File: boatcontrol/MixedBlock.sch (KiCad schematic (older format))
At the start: 2 parts, among them U2501 ULN2803A

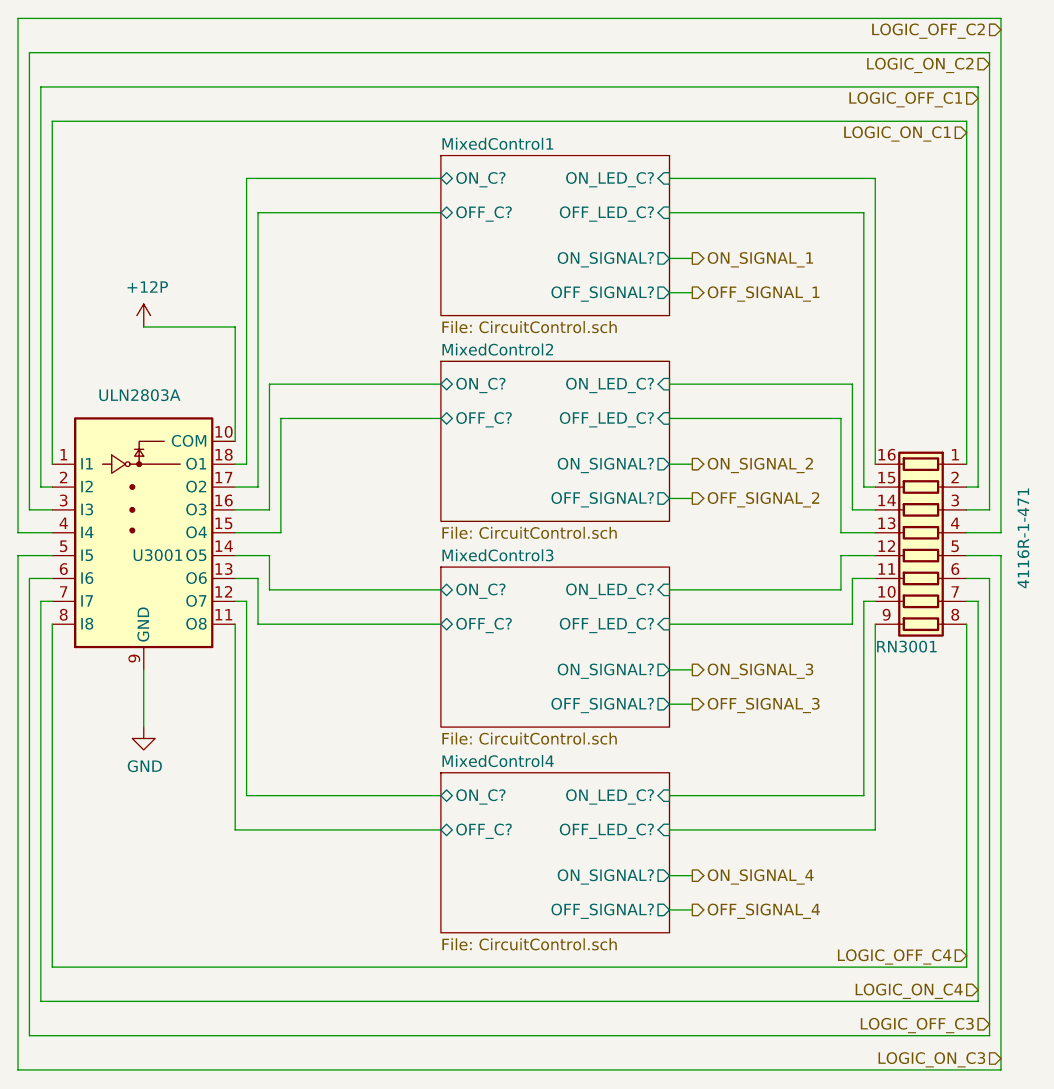
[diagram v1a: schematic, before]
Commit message: Fix extra signals
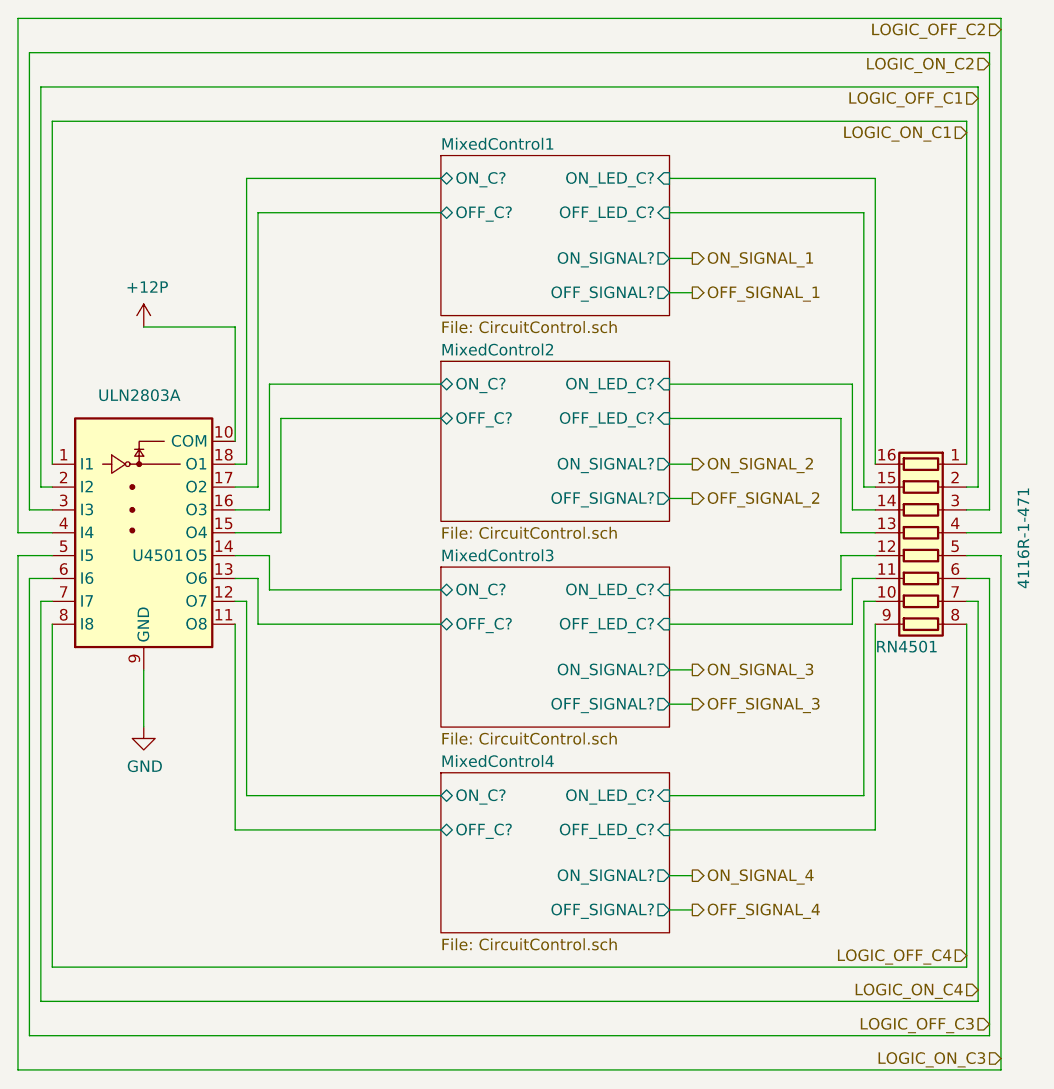
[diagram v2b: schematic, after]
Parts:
- renumbered RN2501 to RN4001, U2501 to U4001
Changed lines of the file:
@@
 AR Path="/E0EE2714/E1383403/E142CD30/D2F31428" Ref="U?"  Part="1"
 AR Path="/E0EE2714/E1383403/E15855D9/D2F31428" Ref="U?"  Part="1"
-AR Path="/E171B33C/E142CD30/D2F31428" Ref="U2501"  Part="1"
-AR Path="/E171B33C/E15855D9/D2F31428" Ref="U3001"  Part="1"
-F 0 "U3001" H 3950 3100 50  0000 L CNN
+AR Path="/E171B33C/E142CD30/D2F31428" Ref="U4001"  Part="1"
+AR Path="/E171B33C/E15855D9/D2F31428" Ref="U4501"  Part="1"
+F 0 "U4501" H 3950 3100 50  0000 L CNN
 F 1 "ULN2803A" H 3800 3800 50  0000 L CNN
 F 2 "Package_DIP:DIP-18_W7.62mm" H 4050 2650 50  0001 L CNN
@@
 AR Path="/E0EE2714/E1383403/E142CD30/5F29B0EF" Ref="#PWR?"  Part="1"
 AR Path="/E0EE2714/E1383403/E15855D9/5F29B0EF" Ref="#PWR?"  Part="1"
-AR Path="/E171B33C/E142CD30/5F29B0EF" Ref="#PWR02502"  Part="1"
-AR Path="/E171B33C/E15855D9/5F29B0EF" Ref="#PWR03002"  Part="1"
-F 0 "#PWR03002" H 4000 4000 50  0001 C CNN
+AR Path="/E171B33C/E142CD30/5F29B0EF" Ref="#PWR04002"  Part="1"
+AR Path="/E171B33C/E15855D9/5F29B0EF" Ref="#PWR04502"  Part="1"
+F 0 "#PWR04502" H 4000 4000 50  0001 C CNN
 F 1 "GND" H 4005 4077 50  0000 C CNN
 F 2 "" H 4000 4250 50  0001 C CNN
@@
 AR Path="/E0EE2714/E1383403/E142CD30/D2B5CDA8" Ref="#PWR?"  Part="1"
 AR Path="/E0EE2714/E1383403/E15855D9/D2B5CDA8" Ref="#PWR?"  Part="1"
-AR Path="/E171B33C/E142CD30/D2B5CDA8" Ref="#PWR02501"  Part="1"
-AR Path="/E171B33C/E15855D9/D2B5CDA8" Ref="#PWR03001"  Part="1"
-F 0 "#PWR03001" H 4000 2350 50  0001 C CNN
+AR Path="/E171B33C/E142CD30/D2B5CDA8" Ref="#PWR04001"  Part="1"
+AR Path="/E171B33C/E15855D9/D2B5CDA8" Ref="#PWR04501"  Part="1"
+F 0 "#PWR04501" H 4000 2350 50  0001 C CNN
 F 1 "+12P" H 4015 2673 50  0000 C CNN
 F 2 "" H 4000 2500 50  0001 C CNN
@@
 AR Path="/E0EE2714/E1383403/E142CD30/D2B5CDA1" Ref="RN?"  Part="1"
 AR Path="/E0EE2714/E1383403/E15855D9/D2B5CDA1" Ref="RN?"  Part="1"
-AR Path="/E171B33C/E142CD30/D2B5CDA1" Ref="RN2501"  Part="1"
-AR Path="/E171B33C/E15855D9/D2B5CDA1" Ref="RN3001"  Part="1"
-F 0 "RN3001" V 7800 3425 50  0000 L CNN
+AR Path="/E171B33C/E142CD30/D2B5CDA1" Ref="RN4001"  Part="1"
+AR Path="/E171B33C/E15855D9/D2B5CDA1" Ref="RN4501"  Part="1"
+F 0 "RN4501" V 7800 3425 50  0000 L CNN
 F 1 "4116R-1-471" H 7100 3050 50  0000 L CNN
 F 2 "BoatControl:DIP254P762X432-16P" V 7875 3500 50  0001 C CNN

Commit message: Cleanup, re-ordering
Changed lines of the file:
@@
 $Descr A4 11693 8268
 encoding utf-8
-Sheet 45 87
+Sheet 40 87
 Title "Boat Control Hat"
 Date "2020-07-09"
@@
 AR Path="/E171B33C/E142CD30/D2F31428" Ref="U4001"  Part="1"
 AR Path="/E171B33C/E15855D9/D2F31428" Ref="U4501"  Part="1"
-F 0 "U4501" H 3950 3100 50  0000 L CNN
+F 0 "U4001" H 3950 3100 50  0000 L CNN
 F 1 "ULN2803A" H 3800 3800 50  0000 L CNN
 F 2 "Package_DIP:DIP-18_W7.62mm" H 4050 2650 50  0001 L CNN
@@
 AR Path="/E171B33C/E142CD30/5F29B0EF" Ref="#PWR04002"  Part="1"
 AR Path="/E171B33C/E15855D9/5F29B0EF" Ref="#PWR04502"  Part="1"
-F 0 "#PWR04502" H 4000 4000 50  0001 C CNN
+F 0 "#PWR04002" H 4000 4000 50  0001 C CNN
 F 1 "GND" H 4005 4077 50  0000 C CNN
 F 2 "" H 4000 4250 50  0001 C CNN
@@
 AR Path="/E171B33C/E142CD30/D2B5CDA8" Ref="#PWR04001"  Part="1"
 AR Path="/E171B33C/E15855D9/D2B5CDA8" Ref="#PWR04501"  Part="1"
-F 0 "#PWR04501" H 4000 2350 50  0001 C CNN
+F 0 "#PWR04001" H 4000 2350 50  0001 C CNN
 F 1 "+12P" H 4015 2673 50  0000 C CNN
 F 2 "" H 4000 2500 50  0001 C CNN
@@
 AR Path="/E171B33C/E142CD30/D2B5CDA1" Ref="RN4001"  Part="1"
 AR Path="/E171B33C/E15855D9/D2B5CDA1" Ref="RN4501"  Part="1"
-F 0 "RN4501" V 7800 3425 50  0000 L CNN
+F 0 "RN4001" V 7800 3425 50  0000 L CNN
 F 1 "4116R-1-471" H 7100 3050 50  0000 L CNN
 F 2 "BoatControl:DIP254P762X432-16P" V 7875 3500 50  0001 C CNN

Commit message: Fix up 10/16A
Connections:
- net MixedControl2/ON_C?: no longer U4001.16 (O3)
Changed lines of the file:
@@
 	4550 3300 4550 2750
-Wire Wire Line
-	4550 2750 5300 2750
 Wire Wire Line
 	4400 3200 4500 3200

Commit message: Cleaner flow
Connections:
- net MixedControl2/DIG_ON: now reaches U4001.16 (O3)
- net MixedControl1/OFF_C? renamed MixedControl1/DIG_OFF
- net MixedControl1/OFF_LED_C? renamed MixedControl1/OFF_LED
- net MixedControl1/ON_C? renamed MixedControl1/DIG_ON
- net MixedControl1/ON_LED_C? renamed MixedControl1/ON_LED
- net MixedControl2/OFF_C? renamed MixedControl2/DIG_OFF
- net MixedControl2/OFF_LED_C? renamed MixedControl2/OFF_LED
- net MixedControl2/ON_LED_C? renamed MixedControl2/ON_LED
- net MixedControl3/OFF_C? renamed MixedControl3/DIG_OFF
- net MixedControl3/OFF_LED_C? renamed MixedControl3/OFF_LED
- net MixedControl3/ON_C? renamed MixedControl3/DIG_ON
- net MixedControl3/ON_LED_C? renamed MixedControl3/ON_LED
- net MixedControl4/OFF_C? renamed MixedControl4/DIG_OFF
- net MixedControl4/OFF_LED_C? renamed MixedControl4/OFF_LED
- net MixedControl4/ON_C? renamed MixedControl4/DIG_ON
- net MixedControl4/ON_LED_C? renamed MixedControl4/ON_LED
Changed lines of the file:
@@
 $Descr A4 11693 8268
 encoding utf-8
-Sheet 40 87
+Sheet 45 87
 Title "Boat Control Hat"
 Date "2020-07-09"
@@
 AR Path="/E171B33C/E142CD30/D2F31428" Ref="U4001"  Part="1"
 AR Path="/E171B33C/E15855D9/D2F31428" Ref="U4501"  Part="1"
-F 0 "U4001" H 3950 3100 50  0000 L CNN
+F 0 "U4501" H 3950 3100 50  0000 L CNN
 F 1 "ULN2803A" H 3800 3800 50  0000 L CNN
 F 2 "Package_DIP:DIP-18_W7.62mm" H 4050 2650 50  0001 L CNN
@@
 AR Path="/E171B33C/E142CD30/5F29B0EF" Ref="#PWR04002"  Part="1"
 AR Path="/E171B33C/E15855D9/5F29B0EF" Ref="#PWR04502"  Part="1"
-F 0 "#PWR04002" H 4000 4000 50  0001 C CNN
+F 0 "#PWR04502" H 4000 4000 50  0001 C CNN
 F 1 "GND" H 4005 4077 50  0000 C CNN
 F 2 "" H 4000 4250 50  0001 C CNN
@@
 AR Path="/E171B33C/E142CD30/D2B5CDA8" Ref="#PWR04001"  Part="1"
 AR Path="/E171B33C/E15855D9/D2B5CDA8" Ref="#PWR04501"  Part="1"
-F 0 "#PWR04001" H 4000 2350 50  0001 C CNN
+F 0 "#PWR04501" H 4000 2350 50  0001 C CNN
 F 1 "+12P" H 4015 2673 50  0000 C CNN
 F 2 "" H 4000 2500 50  0001 C CNN
@@
 AR Path="/E171B33C/E142CD30/D2B5CDA1" Ref="RN4001"  Part="1"
 AR Path="/E171B33C/E15855D9/D2B5CDA1" Ref="RN4501"  Part="1"
-F 0 "RN4001" V 7800 3425 50  0000 L CNN
+F 0 "RN4501" V 6850 3350 50  0000 L CNN
 F 1 "4116R-1-471" H 7100 3050 50  0000 L CNN
 F 2 "BoatControl:DIP254P762X432-16P" V 7875 3500 50  0001 C CNN
@@
 F0 "MixedControl1" 50
 F1 "CircuitControl.sch" 50
-F2 "ON_LED_C?" I R 6300 1850 50
-F3 "OFF_LED_C?" I R 6300 2000 50
-F4 "ON_C?" B L 5300 1850 50
-F5 "OFF_C?" B L 5300 2000 50
-F6 "OFF_SIGNAL?" O R 6300 2350 50
-F7 "ON_SIGNAL?" O R 6300 2200 50
-$EndSheet
-$Sheet
-S 5300 2650 1000 700
-U E150AEB9
-F0 "MixedControl2" 50
-F1 "CircuitControl.sch" 50
-F2 "ON_LED_C?" I R 6300 2750 50
-F3 "OFF_LED_C?" I R 6300 2900 50
-F4 "ON_C?" B L 5300 2750 50
-F5 "OFF_C?" B L 5300 2900 50
-F6 "OFF_SIGNAL?" O R 6300 3250 50
-F7 "ON_SIGNAL?" O R 6300 3100 50
+F2 "ON_LED" I R 6300 1850 50
+F3 "OFF_LED" I R 6300 2000 50
+F4 "DIG_ON" B L 5300 1850 50
+F5 "DIG_OFF" B L 5300 2000 50
+F6 "OFF" O R 6300 2350 50
+F7 "ON" O R 6300 2200 50
 $EndSheet
 $Sheet
@@
 F0 "MixedControl3" 50
 F1 "CircuitControl.sch" 50
-F2 "ON_LED_C?" I R 6300 3650 50
-F3 "OFF_LED_C?" I R 6300 3800 50
-F4 "ON_C?" B L 5300 3650 50
-F5 "OFF_C?" B L 5300 3800 50
-F6 "OFF_SIGNAL?" O R 6300 4150 50
-F7 "ON_SIGNAL?" O R 6300 4000 50
+F2 "ON_LED" I R 6300 3650 50
+F3 "OFF_LED" I R 6300 3800 50
+F4 "DIG_ON" B L 5300 3650 50
+F5 "DIG_OFF" B L 5300 3800 50
+F6 "OFF" O R 6300 4150 50
+F7 "ON" O R 6300 4000 50
 $EndSheet
 $Sheet
@@
 F0 "MixedControl4" 50
 F1 "CircuitControl.sch" 50
-F2 "ON_LED_C?" I R 6300 4550 50
-F3 "OFF_LED_C?" I R 6300 4700 50
-F4 "ON_C?" B L 5300 4550 50
-F5 "OFF_C?" B L 5300 4700 50
-F6 "OFF_SIGNAL?" O R 6300 5050 50
-F7 "ON_SIGNAL?" O R 6300 4900 50
+F2 "ON_LED" I R 6300 4550 50
+F3 "OFF_LED" I R 6300 4700 50
+F4 "DIG_ON" B L 5300 4550 50
+F5 "DIG_OFF" B L 5300 4700 50
+F6 "OFF" O R 6300 5050 50
+F7 "ON" O R 6300 4900 50
 $EndSheet
 Text HLabel 6400 2200 2    50   Output ~ 0
@@
 Wire Wire Line
 	6300 5050 6400 5050
+$Sheet
+S 5300 2650 1000 700
+U E150AEB9
+F0 "MixedControl2" 50
+F1 "CircuitControl.sch" 50
+F2 "ON_LED" I R 6300 2750 50
+F3 "OFF_LED" I R 6300 2900 50
+F4 "DIG_ON" B L 5300 2750 50
+F5 "DIG_OFF" B L 5300 2900 50
+F6 "OFF" O R 6300 3250 50
+F7 "ON" O R 6300 3100 50
+$EndSheet
+Wire Wire Line
+	4550 2750 5300 2750
 $EndSCHEMATC

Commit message: Change inductors
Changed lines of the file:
@@
 $Descr A4 11693 8268
 encoding utf-8
-Sheet 45 87
+Sheet 40 87
 Title "Boat Control Hat"
 Date "2020-07-09"
@@
 AR Path="/E171B33C/E142CD30/D2F31428" Ref="U4001"  Part="1"
 AR Path="/E171B33C/E15855D9/D2F31428" Ref="U4501"  Part="1"
-F 0 "U4501" H 3950 3100 50  0000 L CNN
+F 0 "U4001" H 3950 3100 50  0000 L CNN
 F 1 "ULN2803A" H 3800 3800 50  0000 L CNN
 F 2 "Package_DIP:DIP-18_W7.62mm" H 4050 2650 50  0001 L CNN
@@
 AR Path="/E171B33C/E142CD30/5F29B0EF" Ref="#PWR04002"  Part="1"
 AR Path="/E171B33C/E15855D9/5F29B0EF" Ref="#PWR04502"  Part="1"
-F 0 "#PWR04502" H 4000 4000 50  0001 C CNN
+F 0 "#PWR04002" H 4000 4000 50  0001 C CNN
 F 1 "GND" H 4005 4077 50  0000 C CNN
 F 2 "" H 4000 4250 50  0001 C CNN
@@
 AR Path="/E171B33C/E142CD30/D2B5CDA8" Ref="#PWR04001"  Part="1"
 AR Path="/E171B33C/E15855D9/D2B5CDA8" Ref="#PWR04501"  Part="1"
-F 0 "#PWR04501" H 4000 2350 50  0001 C CNN
+F 0 "#PWR04001" H 4000 2350 50  0001 C CNN
 F 1 "+12P" H 4015 2673 50  0000 C CNN
 F 2 "" H 4000 2500 50  0001 C CNN
@@
 AR Path="/E171B33C/E142CD30/D2B5CDA1" Ref="RN4001"  Part="1"
 AR Path="/E171B33C/E15855D9/D2B5CDA1" Ref="RN4501"  Part="1"
-F 0 "RN4501" V 6850 3350 50  0000 L CNN
+F 0 "RN4001" V 6850 3350 50  0000 L CNN
 F 1 "4116R-1-471" H 7100 3050 50  0000 L CNN
 F 2 "BoatControl:DIP254P762X432-16P" V 7875 3500 50  0001 C CNN

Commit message: Swich drivers for big relays
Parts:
- U4001: value ULN2803A -> TBD62783APG; symbol Transistor_Array:ULN2803A -> Transistor_Array:TBD62783A
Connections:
- net +12P: now also U4001.9 (VCC); no longer U4001.10 (COM)
- net GND: now also U4001.10 (GND); no longer U4001.9 (GND)
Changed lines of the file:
@@
 $Descr A4 11693 8268
 encoding utf-8
-Sheet 40 87
+Sheet 45 87
 Title "Boat Control Hat"
 Date "2020-07-09"
@@
 $EndDescr
 $Comp
-L Transistor_Array:ULN2803A U?
+L Transistor_Array:TBD62783A U?
 U 1 1 D2F31428
-P 4000 3300
+P 4000 3400
 AR Path="/D2F31428" Ref="U?"  Part="1"
 AR Path="/8148B1BC/D2F31428" Ref="U?"  Part="1"
@@
 AR Path="/E171B33C/E142CD30/D2F31428" Ref="U4001"  Part="1"
 AR Path="/E171B33C/E15855D9/D2F31428" Ref="U4501"  Part="1"
-F 0 "U4001" H 3950 3100 50  0000 L CNN
-F 1 "ULN2803A" H 3800 3800 50  0000 L CNN
-F 2 "Package_DIP:DIP-18_W7.62mm" H 4050 2650 50  0001 L CNN
-F 3 "http://www.ti.com/lit/ds/symlink/uln2803a.pdf" H 4100 3100 50  0001 C CNN
-	1    4000 3300
+F 0 "U4501" V 4100 3300 50  0000 L CNN
+F 1 "TBD62783APG" V 3850 3150 50  0000 L CNN
+F 2 "Package_DIP:DIP-18_W7.62mm" H 4050 2750 50  0001 L CNN
+F 3 "https://toshiba.semicon-storage.com/info/docget.jsp?did=30523&prodName=TBD62783AFG" H 4100 3200 50  0001 C CNN
+	1    4000 3400
 	1    0    0    -1
 $EndComp
@@
 AR Path="/E171B33C/E142CD30/5F29B0EF" Ref="#PWR04002"  Part="1"
 AR Path="/E171B33C/E15855D9/5F29B0EF" Ref="#PWR04502"  Part="1"
-F 0 "#PWR04002" H 4000 4000 50  0001 C CNN
+F 0 "#PWR04502" H 4000 4000 50  0001 C CNN
 F 1 "GND" H 4005 4077 50  0000 C CNN
 F 2 "" H 4000 4250 50  0001 C CNN
@@
 L power:+12P #PWR?
 U 1 1 D2B5CDA8
-P 4000 2500
+P 4000 2900
 AR Path="/8148B1BC/D2B5CDA8" Ref="#PWR?"  Part="1"
 AR Path="/81CB63BE/D2B5CDA8" Ref="#PWR?"  Part="1"
@@
 AR Path="/E171B33C/E142CD30/D2B5CDA8" Ref="#PWR04001"  Part="1"
 AR Path="/E171B33C/E15855D9/D2B5CDA8" Ref="#PWR04501"  Part="1"
-F 0 "#PWR04001" H 4000 2350 50  0001 C CNN
-F 1 "+12P" H 4015 2673 50  0000 C CNN
-F 2 "" H 4000 2500 50  0001 C CNN
-F 3 "" H 4000 2500 50  0001 C CNN
-	1    4000 2500
+F 0 "#PWR04501" H 4000 2750 50  0001 C CNN
+F 1 "+12P" H 4015 3073 50  0000 C CNN
+F 2 "" H 4000 2900 50  0001 C CNN
+F 3 "" H 4000 2900 50  0001 C CNN
+	1    4000 2900
 	1    0    0    -1
 $EndComp
-Wire Wire Line
-	4400 3000 4400 2500
-Wire Wire Line
-	4400 2500 4000 2500
 Text HLabel 7600 1650 0    50   Input ~ 0
 LOGIC_ON_C1
@@
 AR Path="/E171B33C/E142CD30/D2B5CDA1" Ref="RN4001"  Part="1"
 AR Path="/E171B33C/E15855D9/D2B5CDA1" Ref="RN4501"  Part="1"
-F 0 "RN4001" V 6850 3350 50  0000 L CNN
+F 0 "RN4501" V 6850 3350 50  0000 L CNN
 F 1 "4116R-1-471" H 7100 3050 50  0000 L CNN
 F 2 "BoatControl:DIP254P762X432-16P" V 7875 3500 50  0001 C CNN

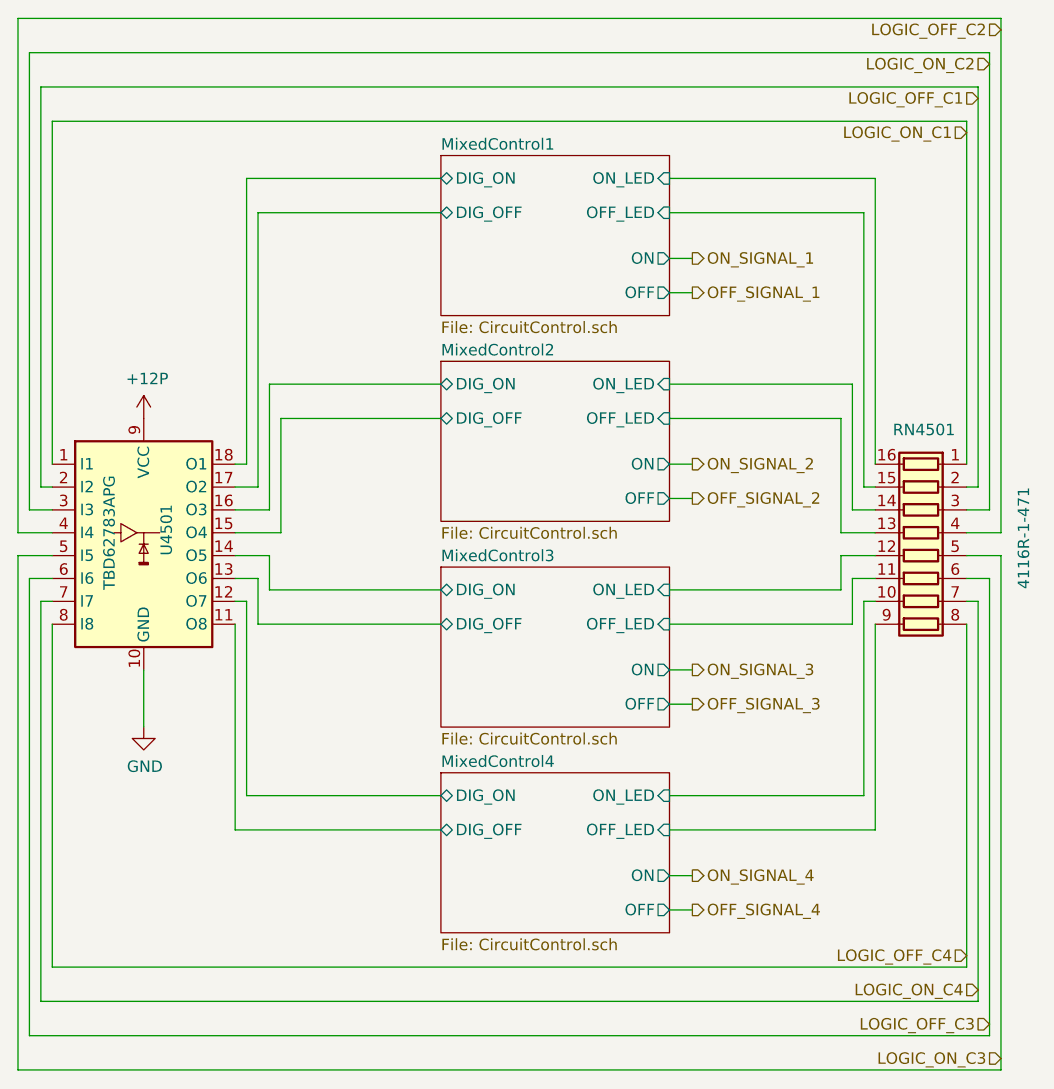
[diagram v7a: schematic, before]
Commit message: Switch resistors
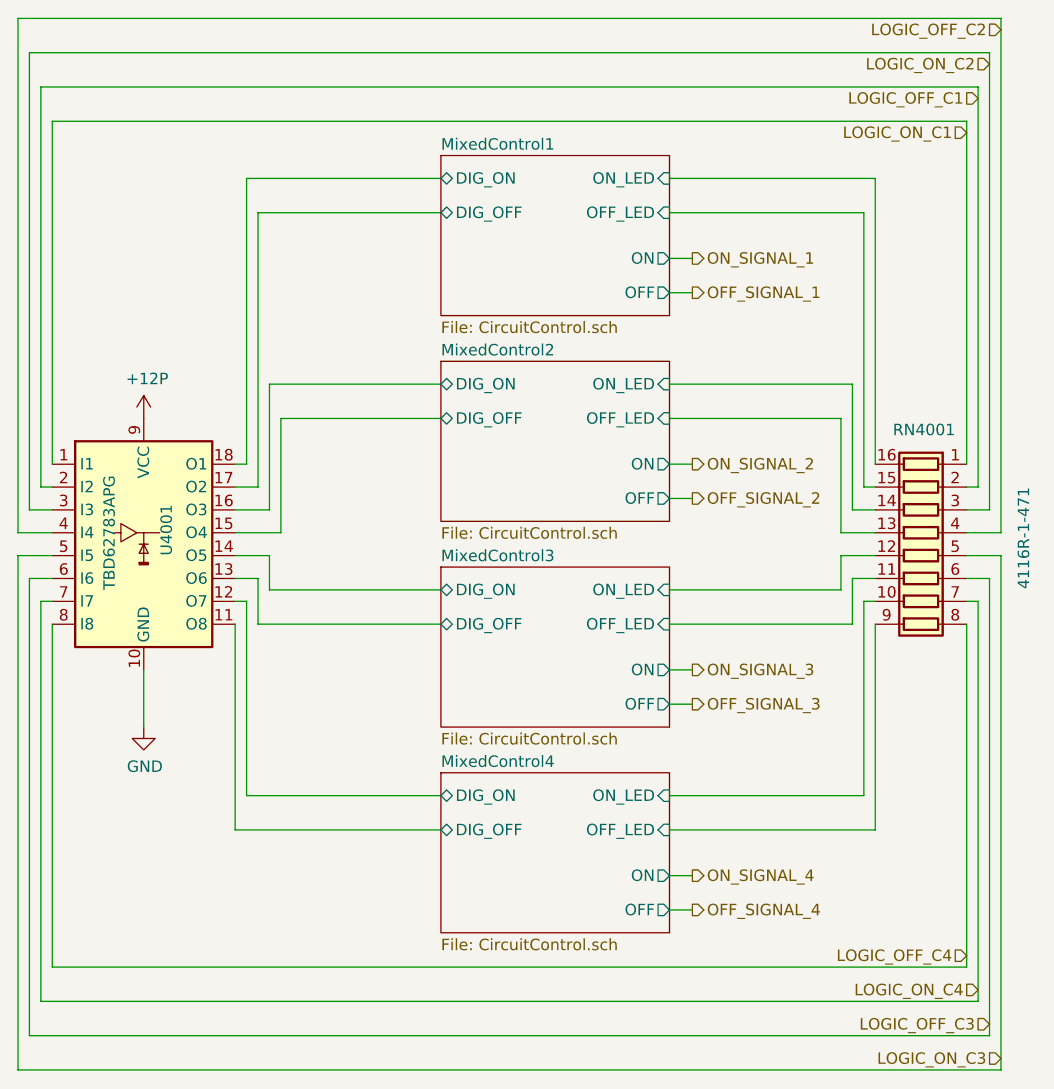
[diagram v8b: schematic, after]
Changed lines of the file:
@@
 $Descr A4 11693 8268
 encoding utf-8
-Sheet 45 87
+Sheet 40 87
 Title "Boat Control Hat"
 Date "2020-07-09"
@@
 AR Path="/E171B33C/E142CD30/D2F31428" Ref="U4001"  Part="1"
 AR Path="/E171B33C/E15855D9/D2F31428" Ref="U4501"  Part="1"
-F 0 "U4501" V 4100 3300 50  0000 L CNN
+F 0 "U4001" V 4100 3300 50  0000 L CNN
 F 1 "TBD62783APG" V 3850 3150 50  0000 L CNN
 F 2 "Package_DIP:DIP-18_W7.62mm" H 4050 2750 50  0001 L CNN
@@
 AR Path="/E171B33C/E142CD30/5F29B0EF" Ref="#PWR04002"  Part="1"
 AR Path="/E171B33C/E15855D9/5F29B0EF" Ref="#PWR04502"  Part="1"
-F 0 "#PWR04502" H 4000 4000 50  0001 C CNN
+F 0 "#PWR04002" H 4000 4000 50  0001 C CNN
 F 1 "GND" H 4005 4077 50  0000 C CNN
 F 2 "" H 4000 4250 50  0001 C CNN
@@
 AR Path="/E171B33C/E142CD30/D2B5CDA8" Ref="#PWR04001"  Part="1"
 AR Path="/E171B33C/E15855D9/D2B5CDA8" Ref="#PWR04501"  Part="1"
-F 0 "#PWR04501" H 4000 2750 50  0001 C CNN
+F 0 "#PWR04001" H 4000 2750 50  0001 C CNN
 F 1 "+12P" H 4015 3073 50  0000 C CNN
 F 2 "" H 4000 2900 50  0001 C CNN
@@
 AR Path="/E171B33C/E142CD30/D2B5CDA1" Ref="RN4001"  Part="1"
 AR Path="/E171B33C/E15855D9/D2B5CDA1" Ref="RN4501"  Part="1"
-F 0 "RN4501" V 6850 3350 50  0000 L CNN
+F 0 "RN4001" V 6850 3350 50  0000 L CNN
 F 1 "4116R-1-471" H 7100 3050 50  0000 L CNN
 F 2 "BoatControl:DIP254P762X432-16P" V 7875 3500 50  0001 C CNN
